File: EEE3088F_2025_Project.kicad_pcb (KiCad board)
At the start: 2 copper layers, 81 x 53.5 mm, 57 parts, among them J1 Conn_02x16_Odd_Even, J2 USB_C_Receptacle_PowerOnly_6P, J3 Conn_01x02, Q2 NMOS, SW1 SW_SPDT, U1 HR8833, U10 INA219AIDCNR, U2 HR8833, U3 MIC2026-1YM, U4 HT7533-1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

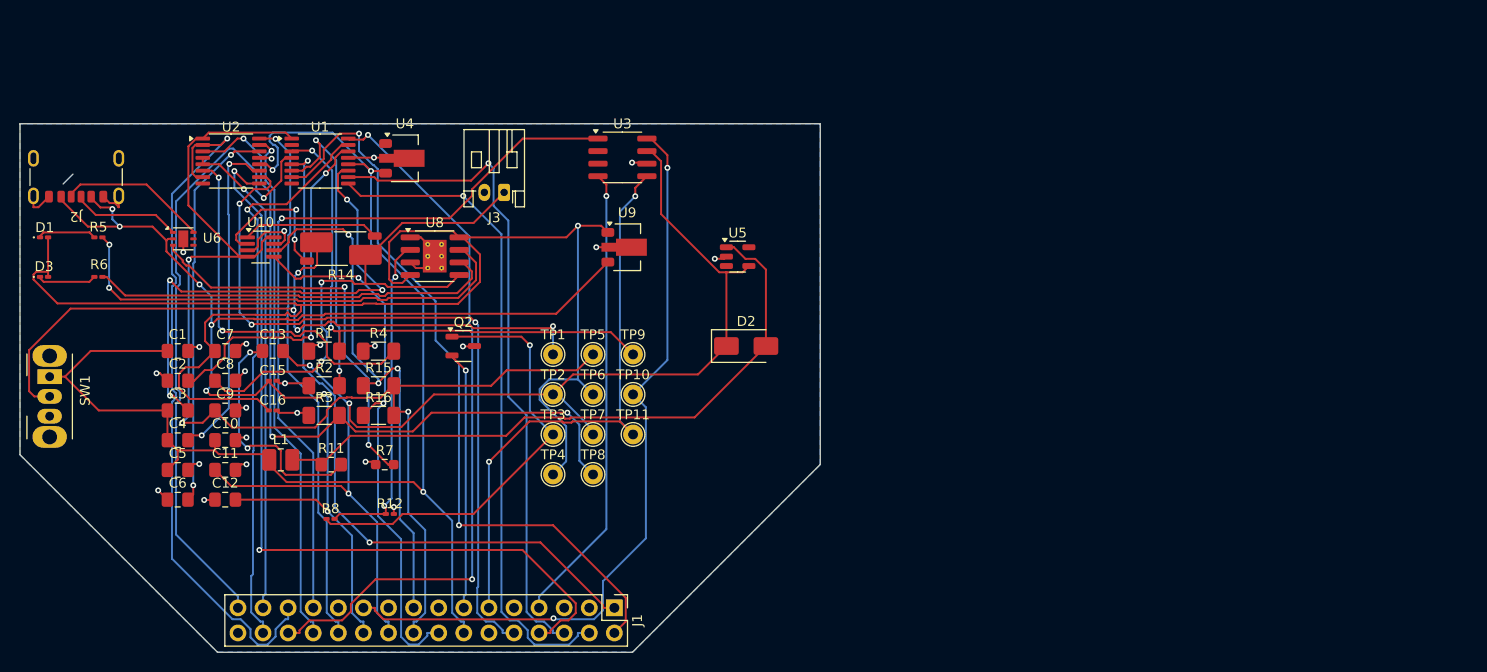
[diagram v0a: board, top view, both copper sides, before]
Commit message: Added mounting holes and solder jumpers
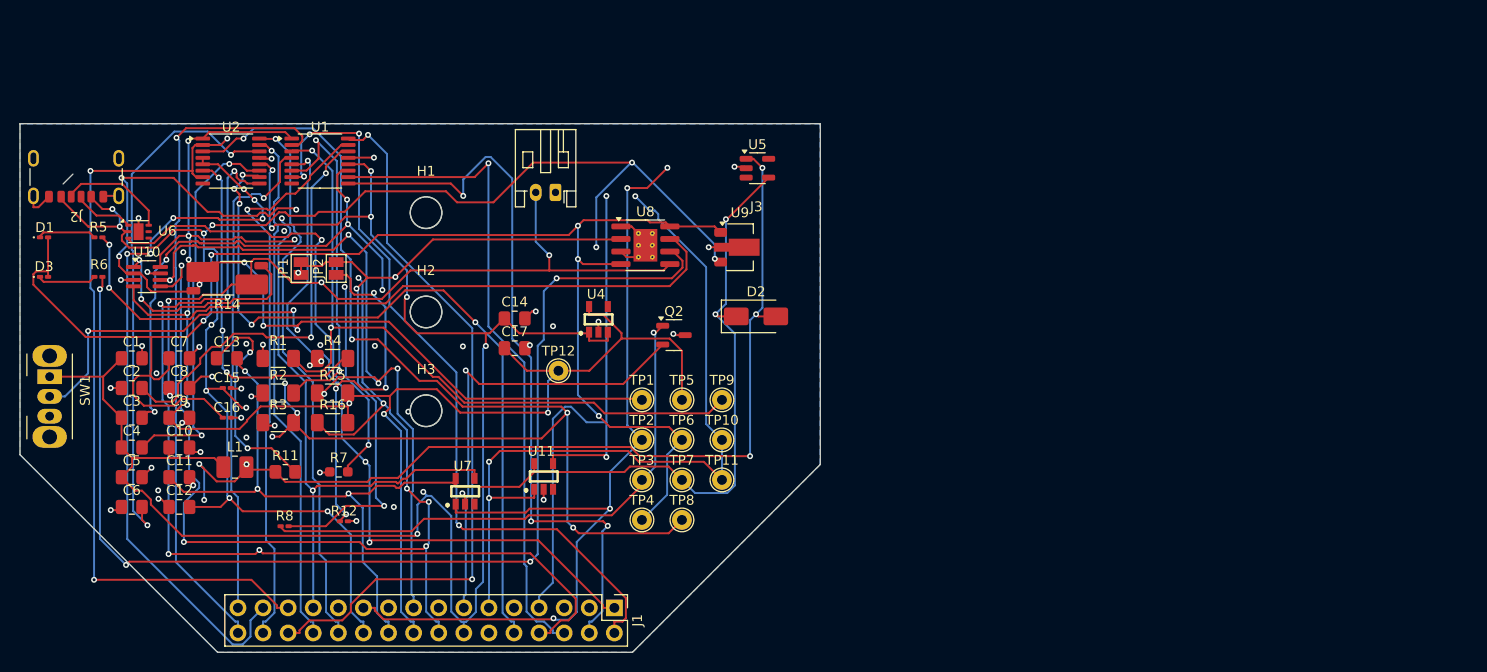
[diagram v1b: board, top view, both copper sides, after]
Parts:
- removed U3: MIC2026-1YM, Package_SO:SOIC-8_3.9x4.9mm_P1.27mm
- added C14: 1u, Capacitor_SMD:C_0805_2012Metric_Pad1.18x1.45mm_HandSolder, F.Cu at (93.6, 95.2)
- added C17: 1u, Capacitor_SMD:C_0805_2012Metric_Pad1.18x1.45mm_HandSolder, F.Cu at (93.6, 98.2)
- added H1: MountingHole, MountingHole:MountingHole_3.2mm_M3, F.Cu at (84.6, 84.5)
- added H2: MountingHole, MountingHole:MountingHole_3.2mm_M3, F.Cu at (84.6, 94.5)
- added H3: MountingHole, MountingHole:MountingHole_3.2mm_M3, F.Cu at (84.6, 104.5)
- added JP1: SolderJumper_2_Open, Jumper:SolderJumper-2_P1.3mm_Open_Pad1.0x1.5mm, F.Cu at (72.0, 90.2)
- added JP2: SolderJumper_2_Open, Jumper:SolderJumper-2_P1.3mm_Open_Pad1.0x1.5mm, F.Cu at (75.5, 90.2)
- added TP12: TestPoint, TestPoint:TestPoint_THTPad_D2.0mm_Drill1.0mm, F.Cu at (98.0, 100.5)
- added U11: AP2171WG-7, Library:SOT-25-5_L2.9-W1.6-P0.95-LS2.8-BL, F.Cu at (96.5, 111.2)
- added U7: AP2171WG-7, Library:SOT-25-5_L2.9-W1.6-P0.95-LS2.8-BL, F.Cu at (88.6, 112.7)
- R12: value 15K -> 5.5K
- R8: value 1.6K -> 1.8K
- U4: value HT7533-1 -> AP2112K-3.3; footprint Package_TO_SOT_SMD:SOT-89-3 -> Library:SOT-25-5_L2.9-W1.6-P0.95-LS2.8-BL
- U5: value TPS613222ADBV -> TPS613222ADBVR
- moved U4 25.5 mm to (102.1, 95.3)
- moved Q2 21.4 mm to (109.7, 96.9)
- moved U8 21.4 mm to (106.8, 87.8)
- moved R14 11.9 mm to (64.5, 91.1)
- moved U10 11.9 mm to (56.4, 91.0)
- moved U9 11.4 mm to (116.4, 88.0)
- moved TP1 10.1 mm to (106.5, 103.5)
- moved TP5 10.1 mm to (110.5, 103.5)
- moved TP9 10.1 mm to (114.5, 103.5)
- moved TP10 10.1 mm to (114.5, 107.5)
- moved TP11 10.1 mm to (114.5, 111.5)
- moved TP2 10.1 mm to (106.5, 107.5)
- moved TP3 10.1 mm to (106.5, 111.5)
- moved TP4 10.1 mm to (106.5, 115.6)
- moved TP6 10.1 mm to (110.5, 107.5)
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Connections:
- net Net-(U10-IN+) renamed /IN+
- net Net-(U10-IN-) renamed /IN-
- J3 pad 1: /Vbat -> GND
- J3 pad 2: GND -> /Vbat
- R12 pad 1: Net-(U8-PROG) -> Net-(JP2-A)
- R8 pad 2: Net-(U8-PROG) -> Net-(JP1-A)
- TP10 pad 1: /EXT_LOAD1_OUT -> /EXT_LOAD2_OUT
- TP2 pad 1: /5V Out -> /EXT_LOAD1_OUT
- U4 pad 1: /3V3 Out -> /Battery
- U8 pad 2: Net-(U8-PROG) -> Net-(JP1-A)
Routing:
- net Net-(U8-~{STDBY}): track 41.6 -> 116.8 mm, vias 0 -> 4
- net Net-(JP1-A): track 0.00 -> 71.6 mm, vias 0 -> 4
- net /MOTOR1_A_OUT: track 0.00 -> 68.4 mm, vias 0 -> 1
- net /I2C1_SCL: track 55.7 -> 106.9 mm, vias 2 -> 7
- net Net-(U2-AISEN): track 75.6 -> 120.5 mm, vias 3 -> 7
- net /Battery: track 132.3 -> 175.8 mm, vias 3 -> 8
- net /3V3 Out: track 126.4 -> 169.9 mm, vias 3 -> 10
- net Net-(JP2-A): track 0.00 -> 35.5 mm, vias 0 -> 4
- net /HV: track 128.0 -> 162.7 mm, vias 7 -> 13
- net Net-(U8-PROG): track 33.5 -> 0.00 mm, vias 2 -> 0
- net Net-(D2-A): track 65.9 -> 97.5 mm, vias 0 -> 6
- net /MOTOR3_B_OUT: track 49.2 -> 75.3 mm, vias 1 -> 6
- net /IN-: track 14.8 -> 38.5 mm, vias 2 -> 3
- net Net-(U8-~{CHRG}): track 48.2 -> 71.3 mm
- net /Vbat: track 55.3 -> 76.0 mm, vias 2 -> 4
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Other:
- outline, holes or cut-outs redrawn

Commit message: added routing
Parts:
- removed C10, C9: 10u, Capacitor_SMD:C_0805_2012Metric_Pad1.18x1.45mm_HandSolder
- removed R14: 3m, Resistor_SMD:R_Shunt_Vishay_WSK2512_6332Metric_T2.21mm
- removed TP11, TP5: TestPoint, TestPoint:TestPoint_THTPad_D2.0mm_Drill1.0mm
- added JP3: SolderJumper_2_Open, Jumper:SolderJumper-2_P1.3mm_Open_Pad1.0x1.5mm, F.Cu at (73.2, 85.0)
- added JP4: SolderJumper_2_Open, Jumper:SolderJumper-2_P1.3mm_Open_Pad1.0x1.5mm, F.Cu at (77.3, 115.5)
- added R9: 3m, Library:R2512, F.Cu at (67.4, 102.5)
- H1, H2, H3: footprint MountingHole:MountingHole_3.2mm_M3 -> MountingHole:MountingHole_3.2mm_M3_DIN965_Pad
- R1, R15, R16, R2, R3, R4: footprint Resistor_SMD:R_1206_3216Metric_Pad1.30x1.75mm_HandSolder -> Library:R1206
- moved C1 65.1 mm to (119.0, 110.0)
- moved C2 60.2 mm to (114.5, 110.0)
- moved C5 59.8 mm to (112.0, 94.0)
- moved C6 59.6 mm to (112.0, 97.5)
- moved U2 56.2 mm to (118.6, 95.6)
- moved TP9 54.6 mm to (61.0, 114.0)
- moved U1 51.2 mm to (118.6, 104.1)
- moved D2 50.7 mm to (69.0, 108.3)
- moved U9 50.1 mm to (66.9, 80.0)
- moved C12 47.6 mm to (107.0, 109.5)
- moved C3 46.8 mm to (101.4, 110.0)
- moved C13 46.7 mm to (111.0, 103.0)
- moved U7 40.1 mm to (119.6, 87.2)
- moved C11 39.8 mm to (95.5, 94.0)
- moved U11 39.0 mm to (119.5, 79.7)
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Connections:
- C16 pad 1: /5V -> Net-(JP3-B)
- C17 pad 1: /3V3 Out -> Net-(JP4-B)
- C8 pad 1: /Vbat -> /IN+
- J3 pad 2: /Vbat -> /IN+
- SW1 pad 2: Net-(SW1-B) -> /IN-
- TP1 pad 1: Net-(SW1-B) -> /IN-
- TP12 pad 1: /3V3 Out -> Net-(JP4-B)
- TP6 pad 1: /5V -> Net-(JP3-B)
- U4 pad 5: /3V3 Out -> Net-(JP4-B)
- U8 pad 5: /Vbat -> /IN+
- U9 pad 1: /5V -> Net-(JP3-B)
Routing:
- net /Battery: track 175.8 -> 0.00 mm, vias 8 -> 11
- net /3V3 Out: track 169.9 -> 0.00 mm, vias 10 -> 5
- net /HV: track 162.7 -> 0.00 mm, vias 13 -> 16
- net /5V: track 152.7 -> 0.00 mm, vias 5 -> 10
- net /5V Out: track 129.6 -> 0.00 mm, vias 5 -> 9
- net Net-(U2-AISEN): track 120.5 -> 0.00 mm, vias 7 -> 6
- net Net-(U8-~{STDBY}): track 116.8 -> 0.00 mm, vias 4 -> 7
- net /I2C1_SCL: track 106.9 -> 0.00 mm, vias 7 -> 3
- net /MOTOR4_CTRL1: track 98.9 -> 0.00 mm
- net Net-(D2-A): track 97.5 -> 0.00 mm, vias 6 -> 2
- net /EXT_LOAD1_OUT: track 90.5 -> 0.00 mm, vias 4 -> 7
- net Net-(SW1-B): track 87.0 -> 0.00 mm, vias 5 -> 0
- net /MOTOR3_A_OUT: track 80.5 -> 0.00 mm, vias 3 -> 4
- net /Motor2_A_OUT: track 79.4 -> 0.00 mm, vias 4 -> 8
- net /EXT_LOAD2_OUT: track 78.2 -> 0.00 mm, vias 3 -> 4
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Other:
- board size 81 x 53.5 mm -> 19 x 19 mm

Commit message: Final files used for submission
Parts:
- moved SW1 138.5 mm to (180.9, 67.5), turned to 180 degrees
- moved R16 122.3 mm to (169.5, 86.1)
- moved R15 122.3 mm to (169.5, 82.8)
- moved R1 122.3 mm to (169.5, 69.6)
- moved R2 122.3 mm to (169.5, 72.9)
- moved R3 122.3 mm to (169.5, 76.2)
- moved R4 122.3 mm to (169.5, 79.5)
- moved C8 113.2 mm to (165.5, 96.5)
- moved JP1 112.6 mm to (174.9, 90.7)
- moved TP9 109.6 mm to (164.6, 78.0)
- moved C17 104.8 mm to (170.3, 96.5)
- moved C14 104.4 mm to (170.3, 93.5)
- moved JP3 102.6 mm to (174.9, 97.8), turned to 0 degrees
- moved JP4 98.6 mm to (174.9, 101.4)
- moved JP2 92.8 mm to (174.9, 94.3)
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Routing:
- net GND: track 0.00 -> 368.9 mm, vias 140 -> 12
- net /5V Out: track 0.00 -> 163.7 mm, vias 9 -> 11
- net /HV: track 0.00 -> 146.3 mm, vias 16 -> 5
- net /Battery: track 0.00 -> 144.2 mm, vias 11 -> 7
- net /3V3 Out: track 0.00 -> 133.5 mm, vias 5 -> 8
- net /IN-: track 0.00 -> 116.7 mm, vias 7 -> 4
- net /5V: track 0.00 -> 116.3 mm, vias 10 -> 8
- net Net-(JP3-B): track 0.00 -> 109.8 mm, vias 10 -> 4
- net Net-(JP1-A): track 0.00 -> 103.9 mm, vias 5 -> 4
- net /IN+: track 0.00 -> 95.1 mm, vias 6 -> 4
- net /I2C1_SDA: track 0.00 -> 89.3 mm, vias 3 -> 2
- net /I2C1_SCL: track 0.00 -> 88.4 mm, vias 3 -> 1
- net /Motor2_B_OUT: track 0.00 -> 86.2 mm, vias 5 -> 2
- net Net-(Q2-D): track 0.00 -> 81.0 mm, vias 6 -> 2
- net Net-(U1-BISEN): track 0.00 -> 79.6 mm, vias 5 -> 3
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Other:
- board size 19 x 19 mm -> 80 x 55 mm
- board text added: "SNGKHA008 DLXOTS001 Group 59"
